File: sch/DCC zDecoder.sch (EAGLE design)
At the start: 24 parts, among them IC1 5V, IC2 ULN2803, IC3 ULN2803, X10 22-23-2031, X11 22-23-2031, X12 22-23-2031, X7 22-23-2031, X8 22-23-2031, X9 22-23-2031

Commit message: added values
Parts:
- C1: value (none) -> 2200u 35V
- R1: value (none) -> 4.7k
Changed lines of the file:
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@@
 <part name="B1" library="rectifier" library_urn="urn:adsk.eagle:library:336" deviceset="RB1A" device="" package3d_urn="urn:adsk.eagle:package:23866/1"/>
 <part name="LED1" library="led" library_urn="urn:adsk.eagle:library:259" deviceset="TLLG4400" device="" package3d_urn="urn:adsk.eagle:package:15797/1" value="green"/>
-<part name="C1" library="rcl" library_urn="urn:adsk.eagle:library:334" deviceset="CPOL-EU" device="E5-8.5" package3d_urn="urn:adsk.eagle:package:23374/1"/>
-<part name="R1" library="rcl" library_urn="urn:adsk.eagle:library:334" deviceset="R-EU_" device="0207/10" package3d_urn="urn:adsk.eagle:package:23491/2"/>
+<part name="C1" library="rcl" library_urn="urn:adsk.eagle:library:334" deviceset="CPOL-EU" device="E5-8.5" package3d_urn="urn:adsk.eagle:package:23374/1" value="2200u 35V"/>
+<part name="R1" library="rcl" library_urn="urn:adsk.eagle:library:334" deviceset="R-EU_" device="0207/10" package3d_urn="urn:adsk.eagle:package:23491/2" value="4.7k"/>
 <part name="GND1" library="supply1" library_urn="urn:adsk.eagle:library:371" deviceset="GND" device=""/>
 <part name="ESP1" library="_esp32" deviceset="ESP32-NODEMCU" device=""/>
@@
 <instance part="C1" gate="G$1" x="58.42" y="226.06" smashed="yes">
 <attribute name="NAME" x="59.563" y="226.5426" size="1.778" layer="95"/>
-<attribute name="VALUE" x="59.563" y="221.4626" size="1.778" layer="96"/>
+<attribute name="VALUE" x="55.3974" y="219.583" size="1.778" layer="96" rot="R90"/>
 </instance>
 <instance part="R1" gate="G$1" x="71.12" y="210.82" smashed="yes" rot="R90">

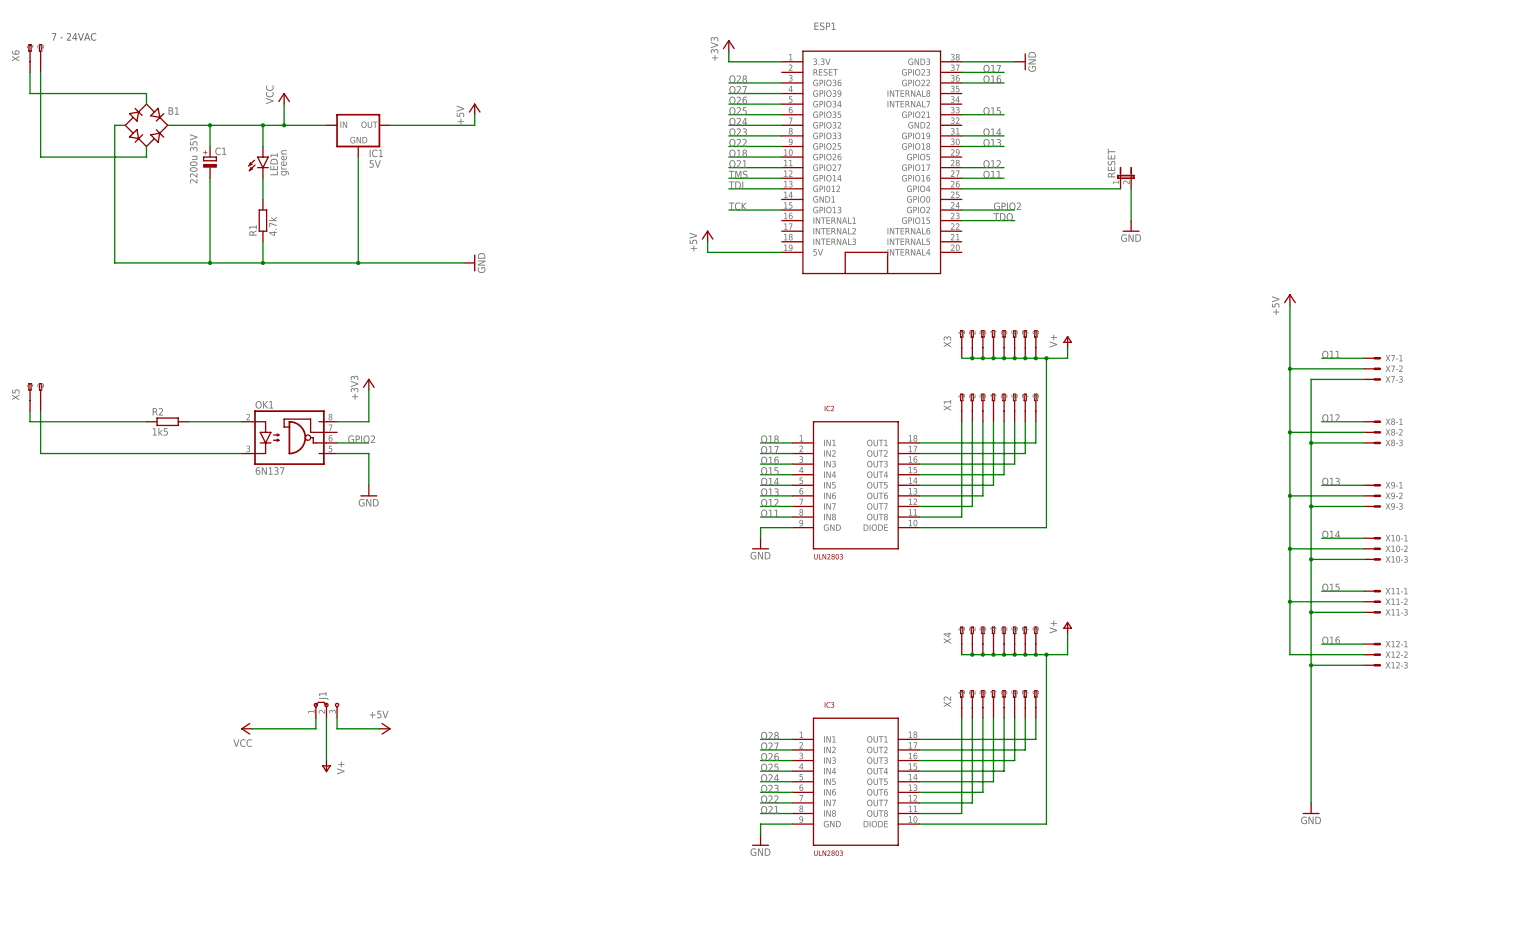
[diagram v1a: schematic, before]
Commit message: reset pin added and pin mapping changed
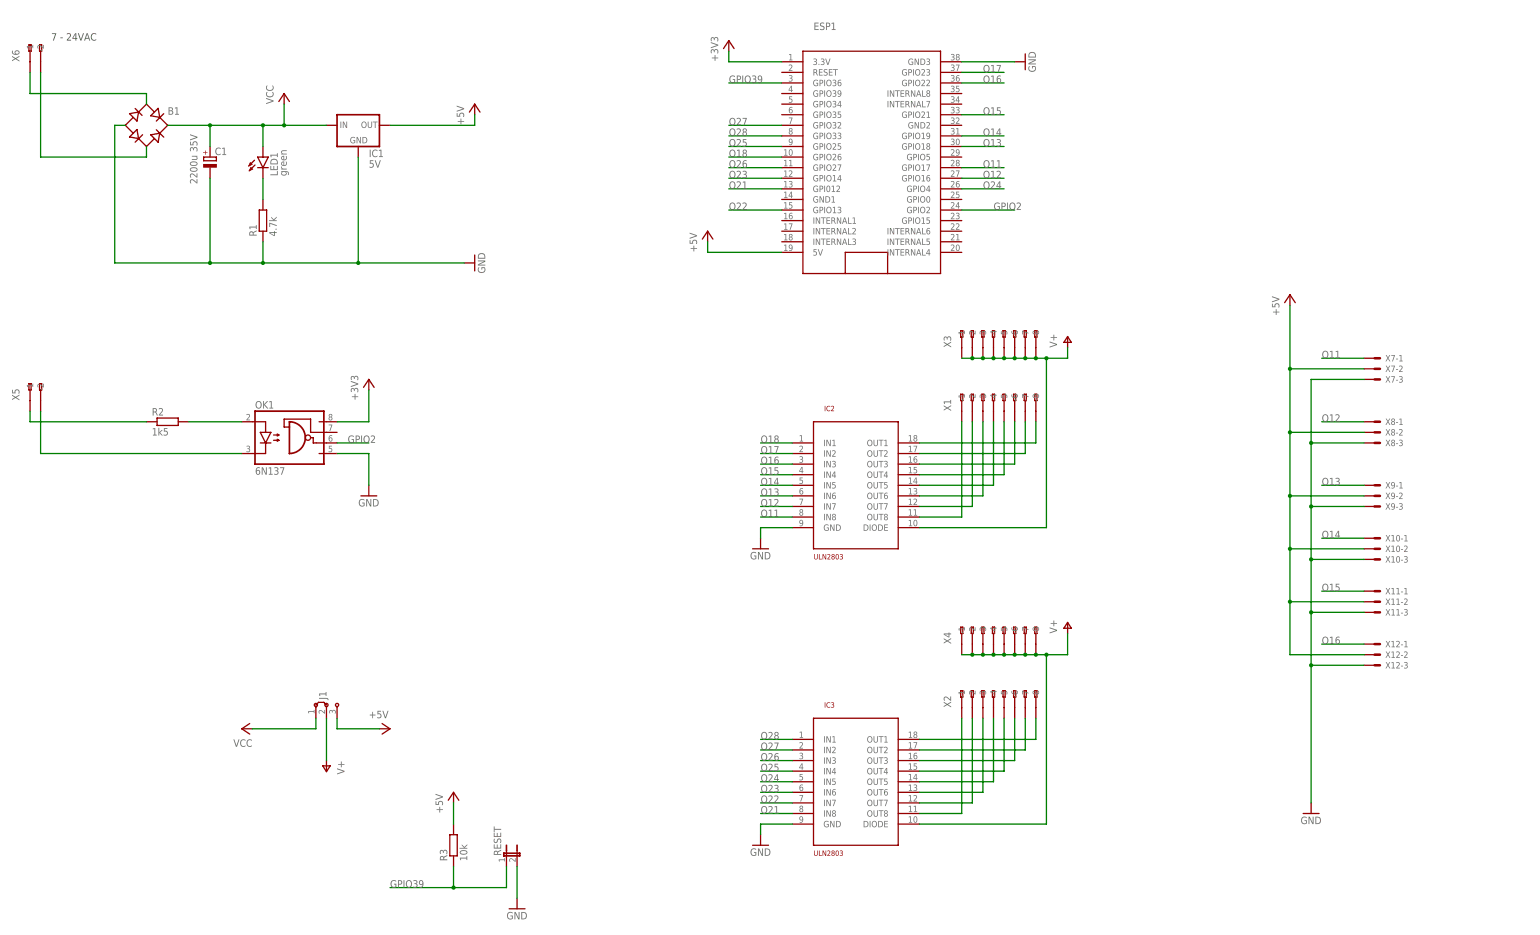
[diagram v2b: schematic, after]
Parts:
- added R3: 10k, rcl:R-EU_0207/10
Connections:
- removed net N$15: ESP1.GPIO4, RESET.1
- removed net TCK: ESP1.GPIO13
- removed net TDI: ESP1.GPI012
- removed net TDO: ESP1.GPIO15
- removed net TMS: ESP1.GPIO14
- new net GPIO39: ESP1.GPIO36, R3.1, RESET.1
- net +5V: now also R3.2
- net O11: now also ESP1.GPIO17; no longer ESP1.GPIO16
- net O12: now also ESP1.GPIO16; no longer ESP1.GPIO17
- net O21: now also ESP1.GPI012; no longer ESP1.GPIO27
- net O22: now also ESP1.GPIO13; no longer ESP1.GPIO25
- net O23: now also ESP1.GPIO14; no longer ESP1.GPIO33
- net O24: now also ESP1.GPIO4; no longer ESP1.GPIO32
- net O25: now also ESP1.GPIO25; no longer ESP1.GPIO35
- net O26: now also ESP1.GPIO27; no longer ESP1.GPIO34
- net O27: now also ESP1.GPIO32; no longer ESP1.GPIO39
- net O28: now also ESP1.GPIO33; no longer ESP1.GPIO36
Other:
- moved on the sheet: RESET

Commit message: partlist updated
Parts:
- B1: value (none) -> B80R DIO
- ESP1: value (none) -> ESP32 NodeMCU
- IC1: value 5V -> TSR 1-2450
- J1: value (none) -> MPE 087-1-003
- LED1: value green -> green 3mm
- RESET: value (none) -> MPE 087-1-002
- X1, X2, X3, X4: value (none) -> DG240 2,54-8
- X10, X11, X12, X7, X8, X9: value 22-23-2031 -> PSS 254/3G
- X5, X6: value (none) -> DG240 2,54-2
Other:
- note added: "DCC"

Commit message: backup
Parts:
- added F1: 900mA, fuse:TE5
- ESP1: value ESP32 NodeMCU -> NodeMCU CH340C; device _esp32:ESP32-NODEMCU -> _esp32:ESP32-NODEMCU-CH340C
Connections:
- new net N$15: F1.1, X6.-1
- net +3V3: now also ESP1.3V3; no longer ESP1.3.3V
- net +5V: now also ESP1.VIN; no longer ESP1.5V
- net GND: now also ESP1.GND0, ESP1.GND1; no longer ESP1.GND3
- net GPIO2: now also ESP1.D2; no longer ESP1.GPIO2
- net GPIO39: now also ESP1.VN; no longer ESP1.GPIO36
- net N$5: now also F1.2; no longer X6.-1
- net O11: now also ESP1.D23; no longer ESP1.GPIO17
- net O12: now also ESP1.D22; no longer ESP1.GPIO16
- net O13: now also ESP1.D21; no longer ESP1.GPIO18
- net O14: now also ESP1.D19; no longer ESP1.GPIO19
- net O15: now also ESP1.D18; no longer ESP1.GPIO21
- net O16: now also ESP1.D17; no longer ESP1.GPIO22
- net O17: now also ESP1.D16; no longer ESP1.GPIO23
- net O18: now also ESP1.D4; no longer ESP1.GPIO26
- net O21: now also ESP1.D32; no longer ESP1.GPI012
- net O22: now also ESP1.D33; no longer ESP1.GPIO13
- net O23: now also ESP1.D26; no longer ESP1.GPIO14
- net O24: now also ESP1.D25; no longer ESP1.GPIO4
- net O25: now also ESP1.D27; no longer ESP1.GPIO25
- net O26: now also ESP1.D14; no longer ESP1.GPIO27
- net O27: now also ESP1.D12; no longer ESP1.GPIO32
- net O28: now also ESP1.D13; no longer ESP1.GPIO33
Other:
- moved on the sheet: B1, C1, IC1, IC2, IC3, J1, LED1, OK1, R1, R2, X1, X2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

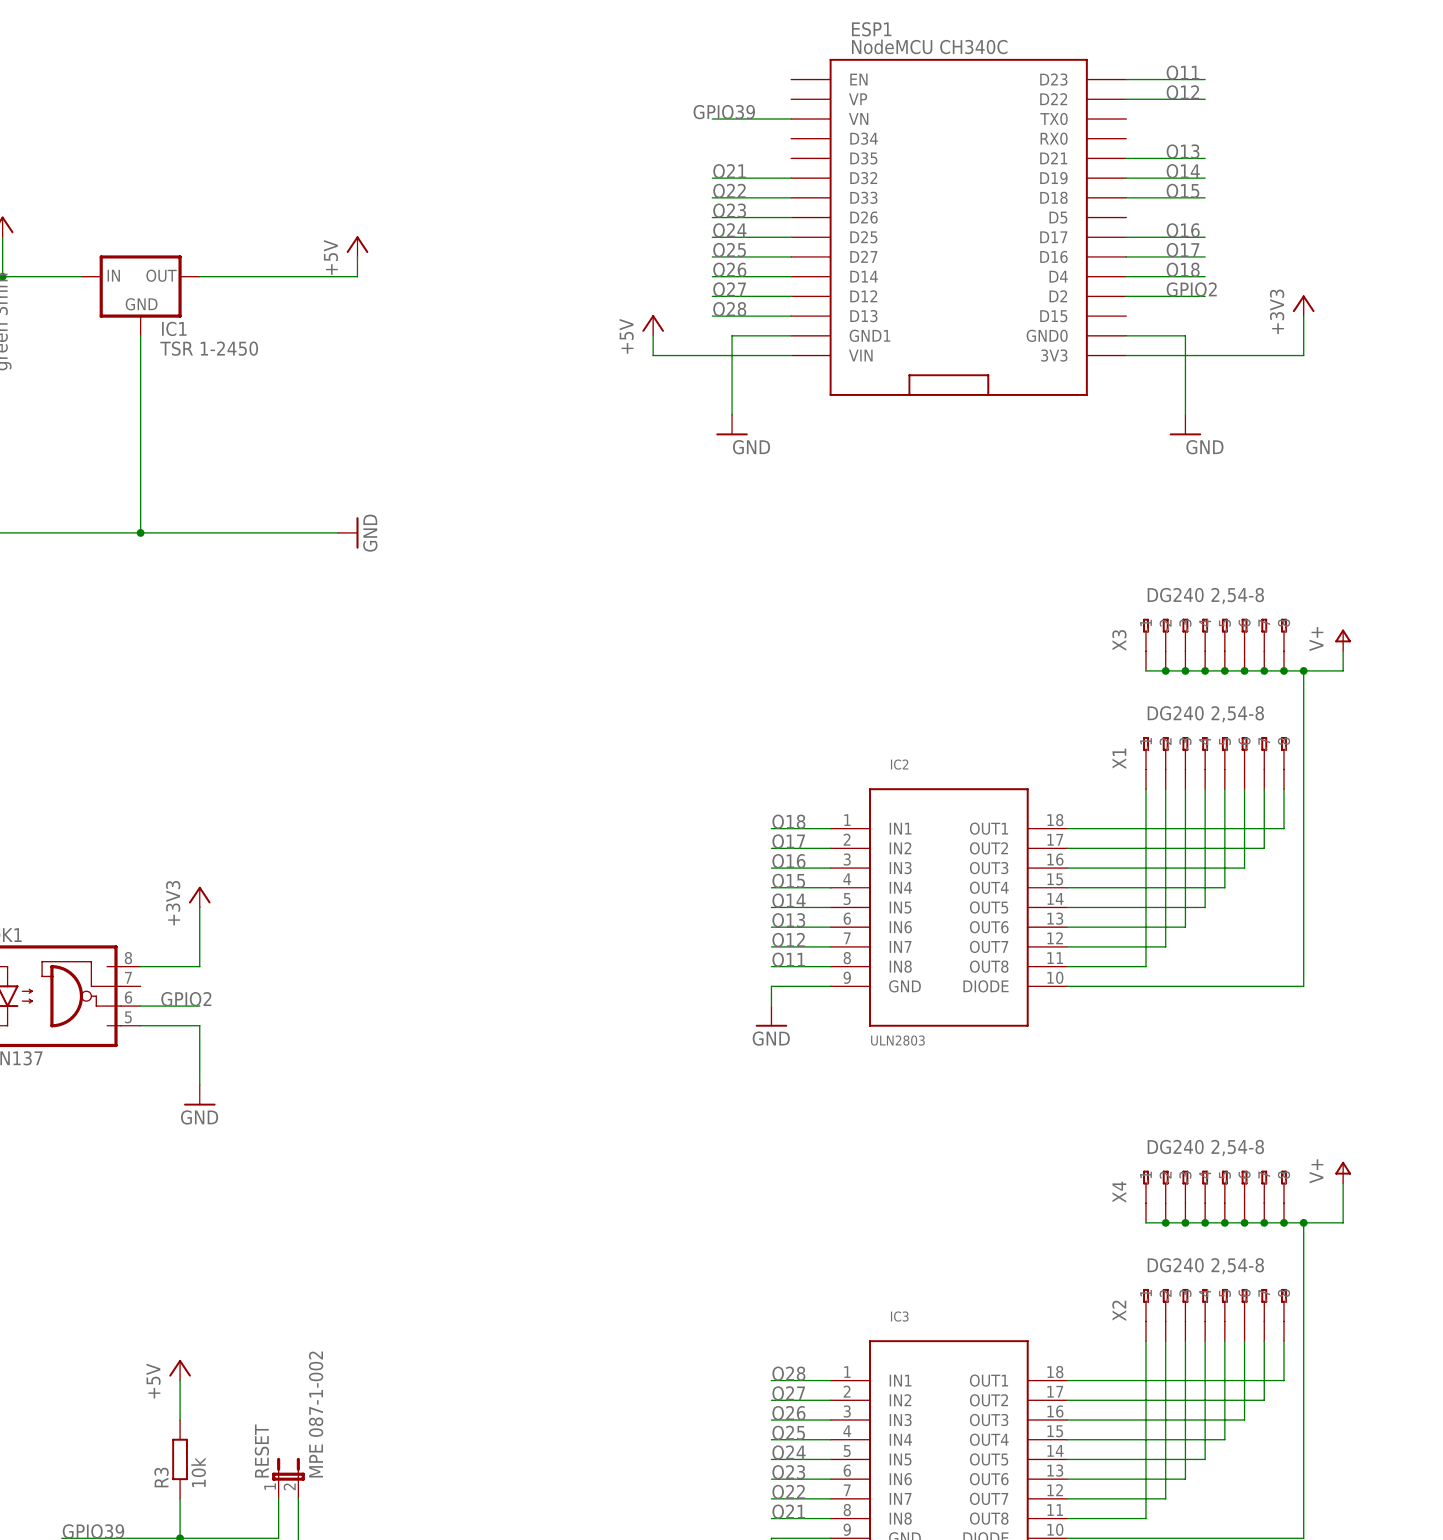
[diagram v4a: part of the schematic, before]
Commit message: routing changed and fuse added
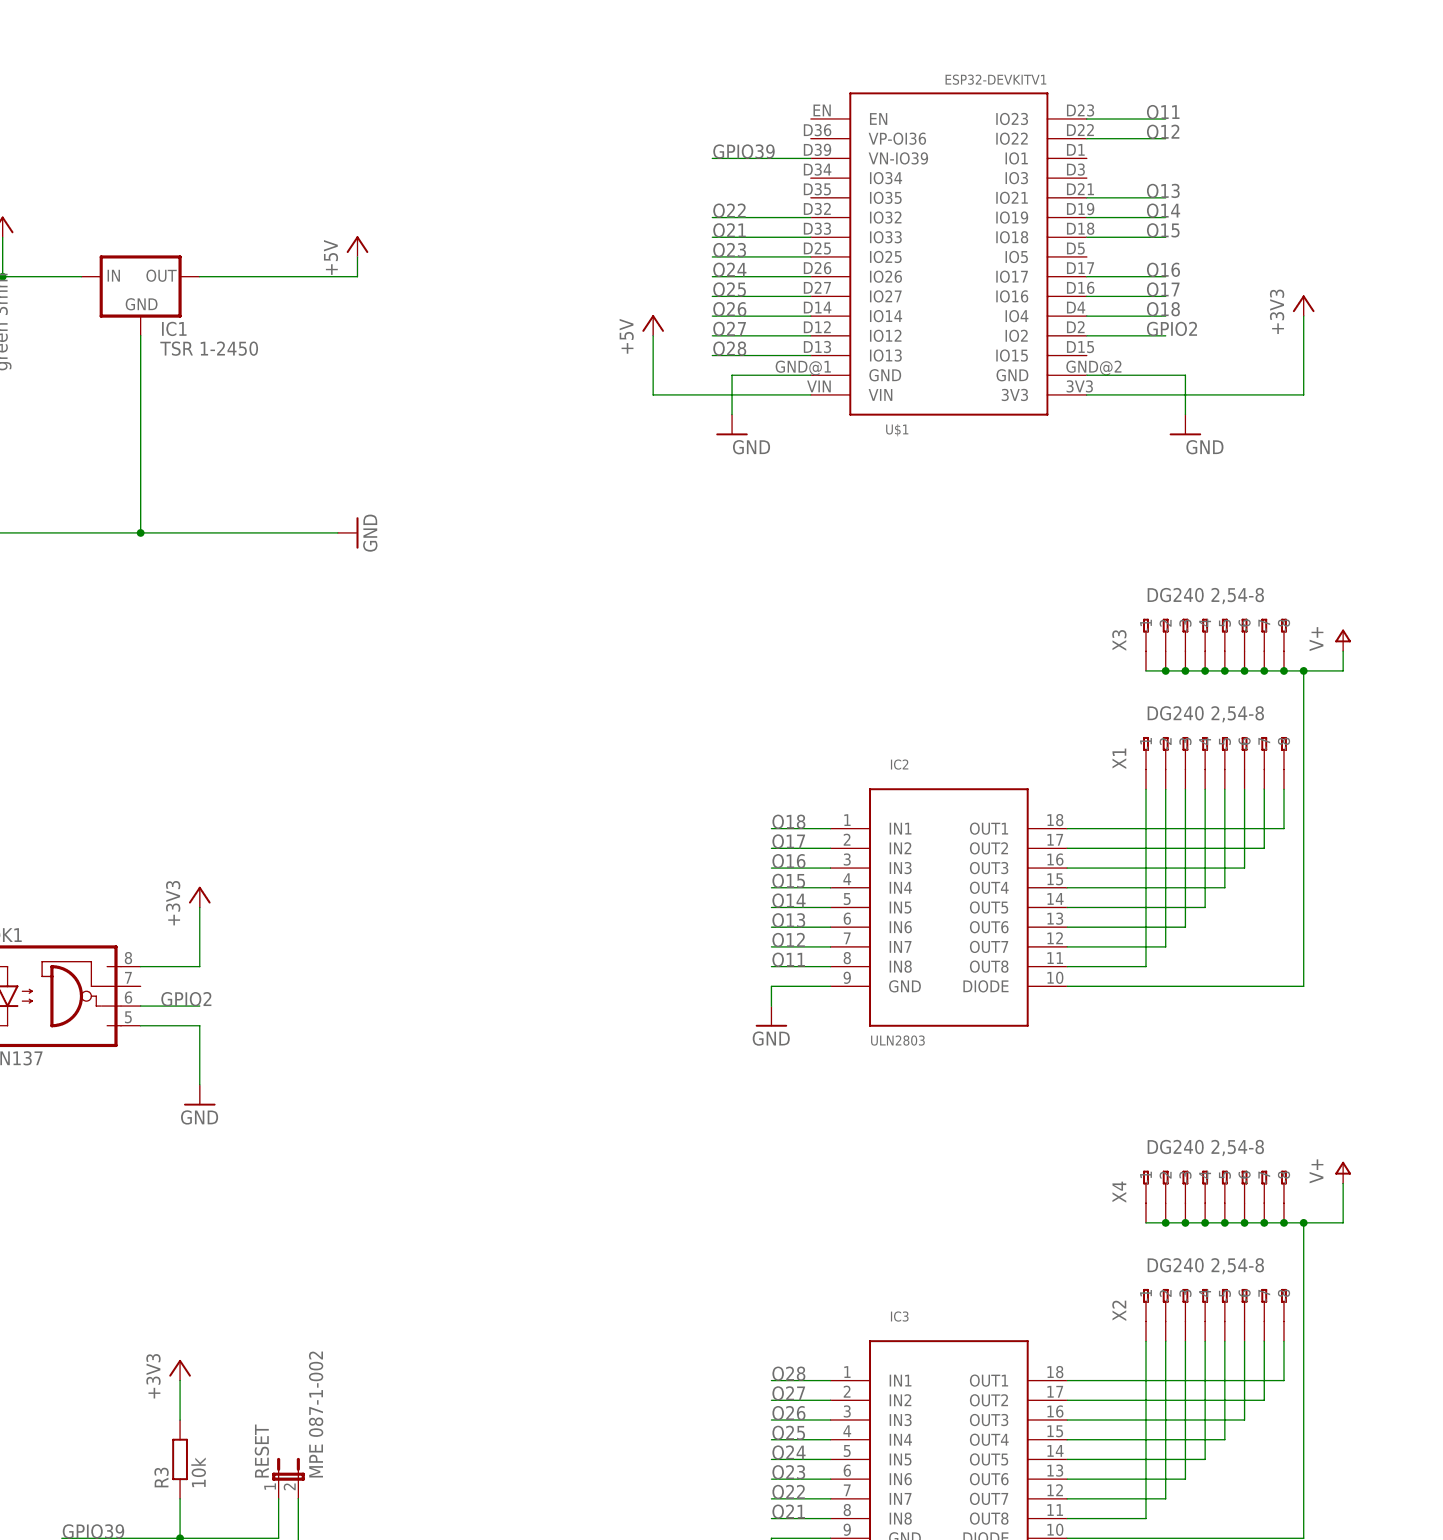
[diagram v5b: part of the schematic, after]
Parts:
- removed ESP1: NodeMCU CH340C, _esp32:ESP32-NODEMCU-CH340C
- added U$1: ESP32DEVKITV1, _esp32:ESP32DEVKITV1
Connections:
- net +3V3: now also R3.2, U$1.3V3; no longer ESP1.3V3
- net +5V: now also U$1.VIN; no longer ESP1.VIN, R3.2
- net GND: now also U$1.GND@1, U$1.GND@2; no longer ESP1.GND0, ESP1.GND1
- net GPIO2: now also U$1.IO2; no longer ESP1.D2
- net GPIO39: now also U$1.VN-IO39; no longer ESP1.VN
- net O11: now also U$1.IO23; no longer ESP1.D23
- net O12: now also U$1.IO22; no longer ESP1.D22
- net O13: now also U$1.IO21; no longer ESP1.D21
- net O14: now also U$1.IO19; no longer ESP1.D19
- net O15: now also U$1.IO18; no longer ESP1.D18
- net O16: now also U$1.IO17; no longer ESP1.D17
- net O17: now also U$1.IO16; no longer ESP1.D16
- net O18: now also U$1.IO4; no longer ESP1.D4
- net O21: now also U$1.IO33; no longer ESP1.D32
- net O22: now also U$1.IO32; no longer ESP1.D33
- net O23: now also U$1.IO25; no longer ESP1.D26
- net O24: now also U$1.IO26; no longer ESP1.D25
- net O25: now also U$1.IO27; no longer ESP1.D27
- net O26: now also U$1.IO14; no longer ESP1.D14
- net O27: now also U$1.IO12; no longer ESP1.D12
- net O28: now also U$1.IO13; no longer ESP1.D13

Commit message: Version 1.0
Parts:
- removed U$1: ESP32DEVKITV1, _esp32:ESP32DEVKITV1
- added C2: 10u, rcl:C-EU050-024X044
- added C3, C4, C5: 100n, rcl:C-EU050-024X044
- added ESP1: ESP32DEVKITV1, _esp32:ESP32DEVKITV1
- IC1: value TSR 1-2450 -> R-78E05-1.0; device v-reg:78XXS -> _eigene:R-78E-XX1.0
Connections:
- net +3V3: now also ESP1.3V3; no longer U$1.3V3
- net +5V: now also C2.1, C3.1, C4.1, C5.1, ESP1.VIN; no longer U$1.VIN
- net GND: now also C2.2, C3.2, C4.2, C5.2, ESP1.GND@1, ESP1.GND@2; no longer U$1.GND@1, U$1.GND@2
- net GPIO2: now also ESP1.IO2; no longer U$1.IO2
- net GPIO39: now also ESP1.VN-IO39; no longer U$1.VN-IO39
- net O11: now also ESP1.IO23; no longer U$1.IO23
- net O12: now also ESP1.IO22; no longer U$1.IO22
- net O13: now also ESP1.IO21; no longer U$1.IO21
- net O14: now also ESP1.IO19; no longer U$1.IO19
- net O15: now also ESP1.IO18; no longer U$1.IO18
- net O16: now also ESP1.IO17; no longer U$1.IO17
- net O17: now also ESP1.IO16; no longer U$1.IO16
- net O18: now also ESP1.IO4; no longer U$1.IO4
- net O21: now also ESP1.IO33; no longer U$1.IO33
- net O22: now also ESP1.IO32; no longer U$1.IO32
- net O23: now also ESP1.IO25; no longer U$1.IO25
- net O24: now also ESP1.IO26; no longer U$1.IO26
- net O25: now also ESP1.IO27; no longer U$1.IO27
- net O26: now also ESP1.IO14; no longer U$1.IO14
- net O27: now also ESP1.IO12; no longer U$1.IO12
- net O28: now also ESP1.IO13; no longer U$1.IO13
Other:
- note added: "nur bestücken wenn Servos verwendet werden"
- moved on the sheet: B1, C1, F1, IC1, LED1, R1, X10-1, X10-2, X10-3, X11-1, X11-2, X11-3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
